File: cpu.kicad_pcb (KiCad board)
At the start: 2 copper layers, 179.6 x 119 mm, 52 parts, among them J1 LCD 2004 Female Header, J2 USB4105-GF-A, SW1 TL2230, U1 LM555, U10 SST39SF040-70-4C-PHE, U2 74LS00, U3 LM555, U4 74LS163, U5 74LS163, U6 74LS163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

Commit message: Adjusted positions of resistors for LEDs. Added Lutzcraft logo to project footprint library.
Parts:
- removed the G*** at (104.8, 71.8)
- added G***: LOGO, footprints:Lutzcraft_logo_1125DPI, B.Cu at (104.1, 71.8)
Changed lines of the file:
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@@
     )
   )
-  (footprint "Lutzcraft:Lutzcraft_logo_1125DPI" (layer "B.Cu")
-    (at 104.775 71.755 180)
+  (footprint "footprints:Lutzcraft_logo_1125DPI" (layer "B.Cu")
+    (at 104.14 71.755 180)
+    (attr board_only exclude_from_bom allow_missing_courtyard)
     (fp_text reference "G***" (at 0 0) (layer "B.SilkS") hide
         (effects (font (size 1.524 1.524) (thickness 0.3)) (justify mirror))

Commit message: Commit to be safe.
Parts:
- moved R2 9.09 mm to (92.1, 127.0), turned to 180 degrees
- moved R9 1.36 mm to (109.2, 123.8)
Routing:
- net Net-(D1-K): track 12.7 -> 5.54 mm
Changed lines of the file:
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@@
   )
   (footprint "Resistor_THT:R_Axial_DIN0207_L6.3mm_D2.5mm_P7.62mm_Horizontal" (layer "F.Cu")
-    (at 83.185 125.095)
+    (at 92.075 127 180)
     (descr "Resistor, Axial_DIN0207 series, Axial, Horizontal, pin pitch=7.62mm, 0.25W = 1/4W, length*diameter=6.3*2.5mm^2, http://cdn-reichelt.de/documents/datenblatt/B400/1_4W%23YAG.pdf")
     (tags "Resistor Axial_DIN0207 series Axial Horizontal pin pitch 7.62mm 0.25W = 1/4W length 6.3mm diameter 2.5mm")
@@
     (property "ki_keywords" "R res resistor")
     (attr through_hole)
-    (fp_text reference "R2" (at 3.81 -2.37) (layer "F.SilkS")
+    (fp_text reference "R2" (at 3.81 2.54) (layer "F.SilkS")
         (effects (font (size 1 1) (thickness 0.15)))
     )
@@
     (fp_line (start 7.62 0) (end 6.96 0)
       (stroke (width 0.1) (type solid)) (layer "F.Fab"))
-    (pad "1" thru_hole circle (at 0 0) (size 1.6 1.6) (drill 0.8) (layers "*.Cu" "*.Mask")
+    (pad "1" thru_hole circle (at 0 0 180) (size 1.6 1.6) (drill 0.8) (layers "*.Cu" "*.Mask")
       (net 2 "GND") (pintype "passive"))
-    (pad "2" thru_hole oval (at 7.62 0) (size 1.6 1.6) (drill 0.8) (layers "*.Cu" "*.Mask")
+    (pad "2" thru_hole oval (at 7.62 0 180) (size 1.6 1.6) (drill 0.8) (layers "*.Cu" "*.Mask")
       (net 7 "Net-(D1-K)") (pintype "passive"))
     (model "${KICAD6_3DMODEL_DIR}/Resistor_THT.3dshapes/R_Axial_DIN0207_L6.3mm_D2.5mm_P7.62mm_Horizontal.wrl"
@@
   )
   (footprint "Resistor_THT:R_Axial_DIN0207_L6.3mm_D2.5mm_P7.62mm_Horizontal" (layer "F.Cu")
-    (at 109.733 122.565 180)
+    (at 109.22 123.825 180)
     (descr "Resistor, Axial_DIN0207 series, Axial, Horizontal, pin pitch=7.62mm, 0.25W = 1/4W, length*diameter=6.3*2.5mm^2, http://cdn-reichelt.de/documents/datenblatt/B400/1_4W%23YAG.pdf")
     (tags "Resistor Axial_DIN0207 series Axial Horizontal pin pitch 7.62mm 0.25W = 1/4W length 6.3mm diameter 2.5mm")
@@
   (segment (start 133.355 123.058) (end 131.572 124.841) (width 0.25) (layer "F.Cu") (net 6))
   (segment (start 133.355 120.533) (end 133.355 123.058) (width 0.25) (layer "F.Cu") (net 6))
-  (segment (start 79.31 127.925) (end 86.07 127.925) (width 0.3) (layer "F.Cu") (net 7))
-  (segment (start 86.07 127.925) (end 88.9 125.095) (width 0.3) (layer "F.Cu") (net 7))
-  (segment (start 79.3 127.935) (end 79.31 127.925) (width 0.3) (layer "F.Cu") (net 7))
-  (segment (start 88.9 125.095) (end 90.805 125.095) (width 0.3) (layer "F.Cu") (net 7))
+  (segment (start 79.3 127.935) (end 80.235 127) (width 0.3) (layer "F.Cu") (net 7))
+  (segment (start 80.235 127) (end 84.455 127) (width 0.3) (layer "F.Cu") (net 7))
   (segment (start 110.069 139.66) (end 100.584 130.175) (width 0.3) (layer "F.Cu") (net 8))
   (segment (start 68.834 129.957) (end 67.056 131.735) (width 0.3) (layer "F.Cu") (net 8))
@@
   (segment (start 126.54 134.33) (end 126.83 134.62) (width 0.25) (layer "B.Cu") (net 9))
   (segment (start 215.9 92.71) (end 215.9 98.811) (width 0.25) (layer "F.Cu") (net 10))
-  (segment (start 104.775 125.227) (end 102.113 122.565) (width 0.3) (layer "F.Cu") (net 11))
+  (segment (start 103.373 123.825) (end 101.6 123.825) (width 0.3) (layer "F.Cu") (net 11))
   (segment (start 104.775 128.661) (end 104.775 125.227) (width 0.3) (layer "F.Cu") (net 11))
+  (segment (start 104.775 125.227) (end 103.373 123.825) (width 0.3) (layer "F.Cu") (net 11))
   (segment (start 138.2522 39.878) (end 138.2522 43.9346) (width 0.25) (layer "F.Cu") (net 12))
   (segment (start 112.258 128.661) (end 114.046 126.873) (width 0.3) (layer "F.Cu") (net 12))

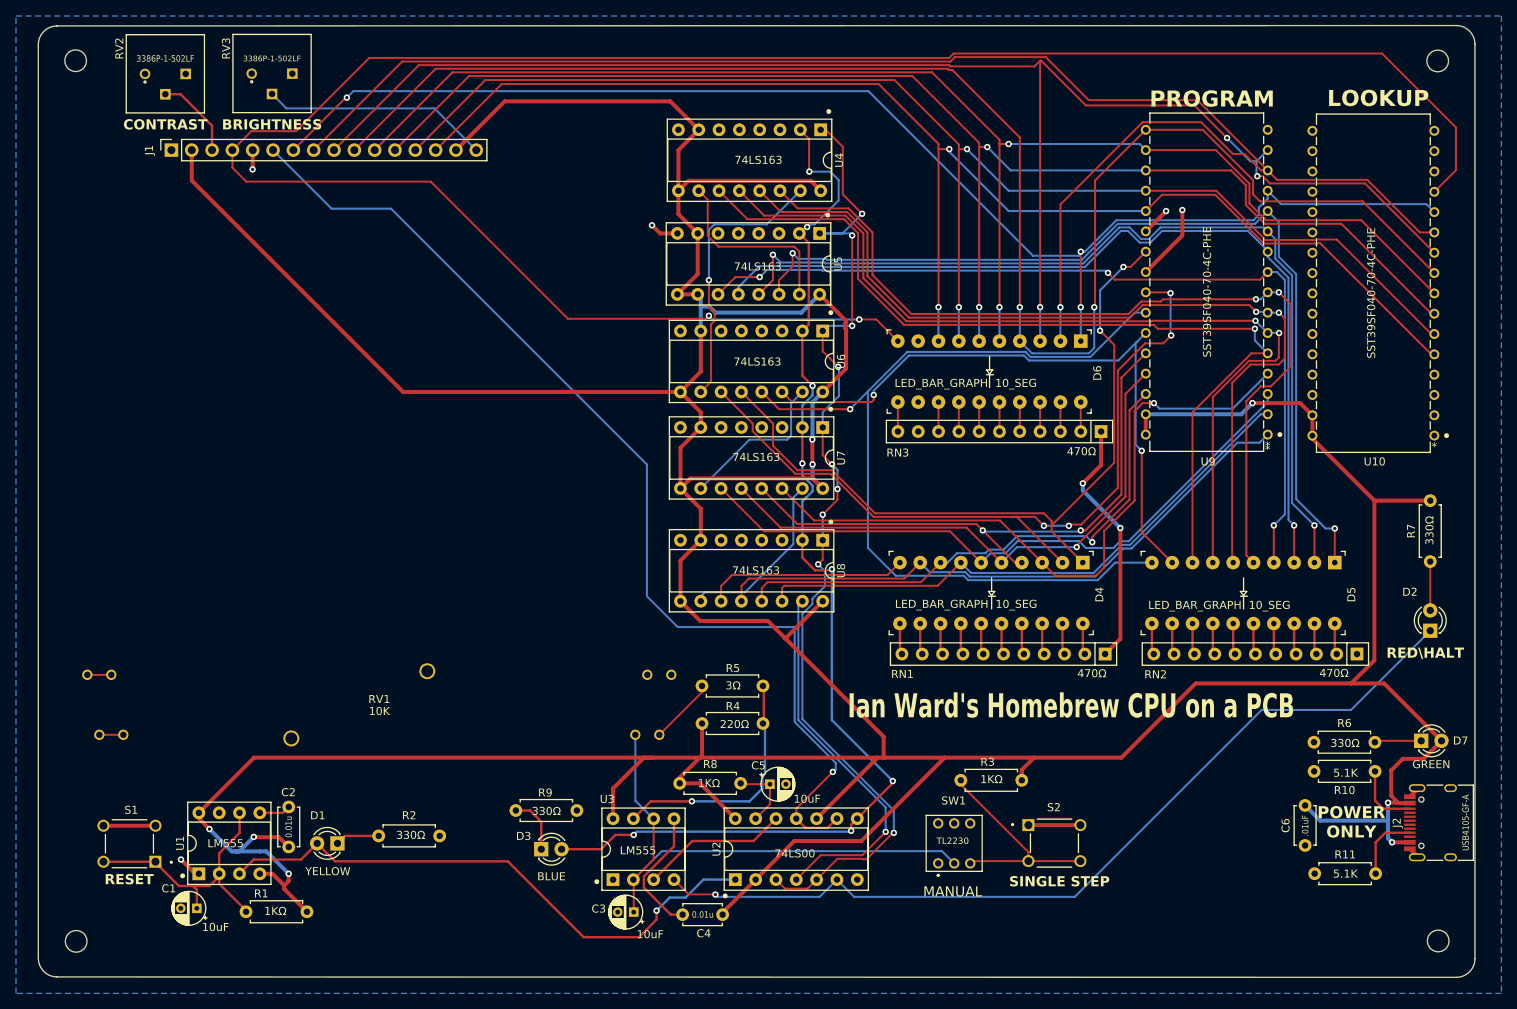
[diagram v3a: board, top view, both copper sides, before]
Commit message: Changed out USB connector for new power-only version with fewer pins. Generated new gerber/drill files.
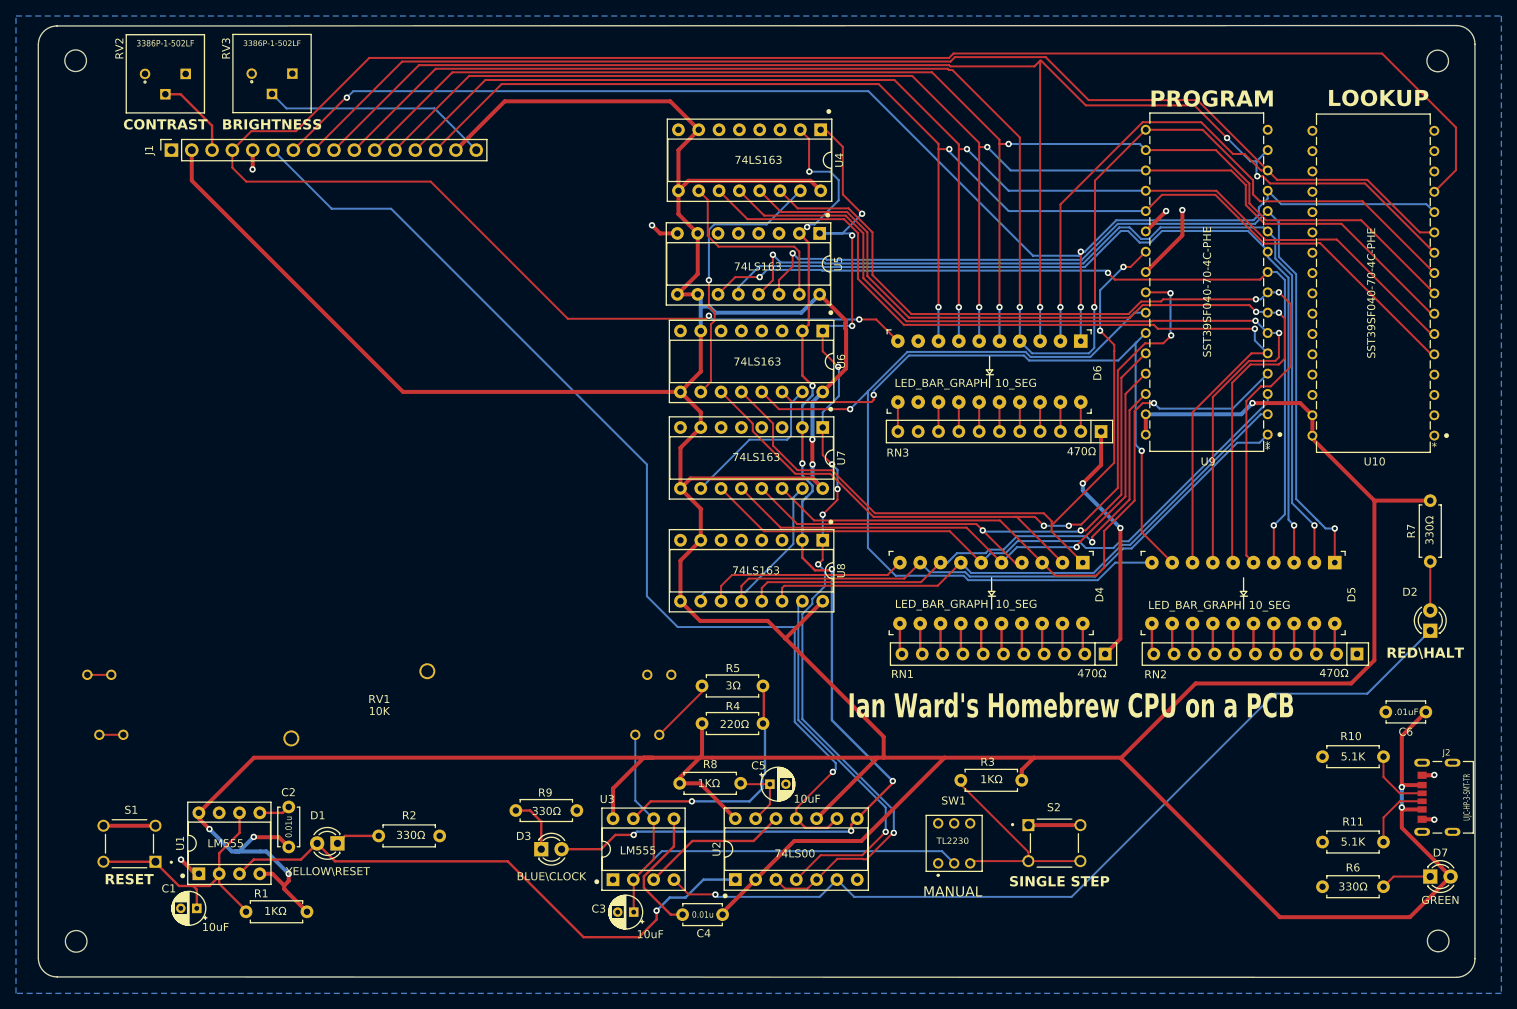
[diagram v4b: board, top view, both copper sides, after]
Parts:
- D1: value YELLOW -> YELLOW\RESET
- D3: value BLUE -> BLUE\CLOCK
- J2: value USB4105-GF-A -> UJC-HP-3-SMT-TR; footprint footprints:USB_C_Receptacle_HRO_TYPE-C-31-M-12 -> footprints:CUI_UJC-HP-3-SMT-TR
- moved C6 19.1 mm to (215.3, 111.5), turned to 180 degrees
- moved R6 18.1 mm to (202.4, 133.4)
- moved D7 17.0 mm to (215.9, 132.1)
- moved R11 9.47 mm to (210.1, 127.8), turned to 180 degrees
- moved J2 4.05 mm to (214.9, 122.2)
- moved R10 2.11 mm to (210.1, 117.1)
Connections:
- J2 pad A5: Net-(J2-PadA5) -> Net-(J2-CC1)
- J2 pad S1: GND -> unconnected-(J2-SHIELD-PadS1)
- R11 pad 1: GND -> Net-(J2-CC1)
- R11 pad 2: Net-(J2-PadA5) -> GND
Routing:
- net +5V: track 682.5 -> 715.9 mm
- net Net-(J2-CC1): track 0.00 -> 8.72 mm
- net Net-(J2-PadA5): track 8.68 -> 0.00 mm
- net Net-(D7-K): track 5.86 -> 6.37 mm
- net GND: track 69.6 -> 69.8 mm, vias 7 -> 9
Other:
- board text added: "${project_name} Inspired by Ian Ward (www excess.org) YouTube Channel: https://www.youtube.com/@IanWard1 PCB designed by one of his appreciative YouTube subscribers. Version ${version} 3/17/2024"
- board text removed: "${project_name} Inspired by Ian Ward (www excess.org) YouTube Channel: https://www.youtube.com/@IanWard1 PCB designed by one of his appreciative YouTube subscribers. Version ${version} 3/6/2024"
- board text removed: "POWER ONLY"
